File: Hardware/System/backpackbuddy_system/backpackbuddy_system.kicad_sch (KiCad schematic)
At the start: 27 parts, among them J1 PIR, J2 Ultrasonic 2, J3 Ultrasonic 1, J4 Left Vibration 1, J5 Left Vibration 2, J6 Raspberry Pi, J7 ESP8266, J8 Right Vibration 1, J9 Right Vibration 2, Q1 Q_NMOS_GSD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

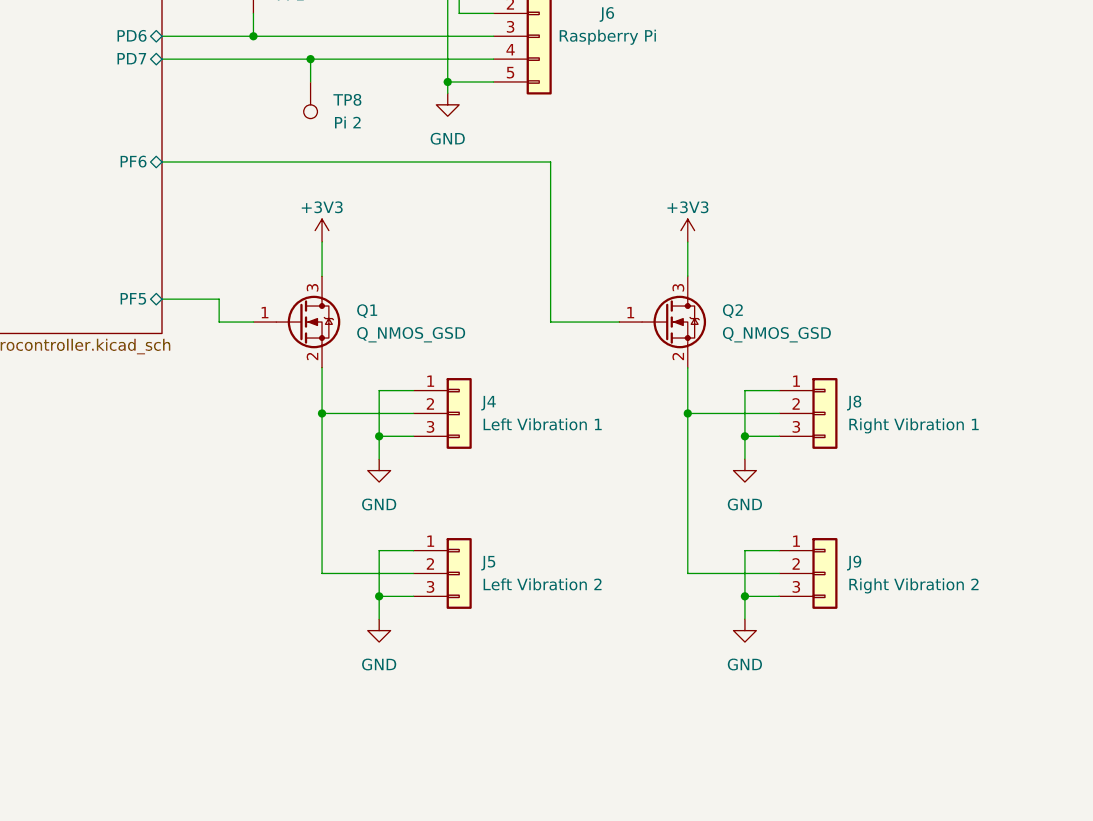
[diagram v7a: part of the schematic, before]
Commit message: changed D1, the MCU reset switch diode from 50V to 1V, changed crystal caps to 22pF
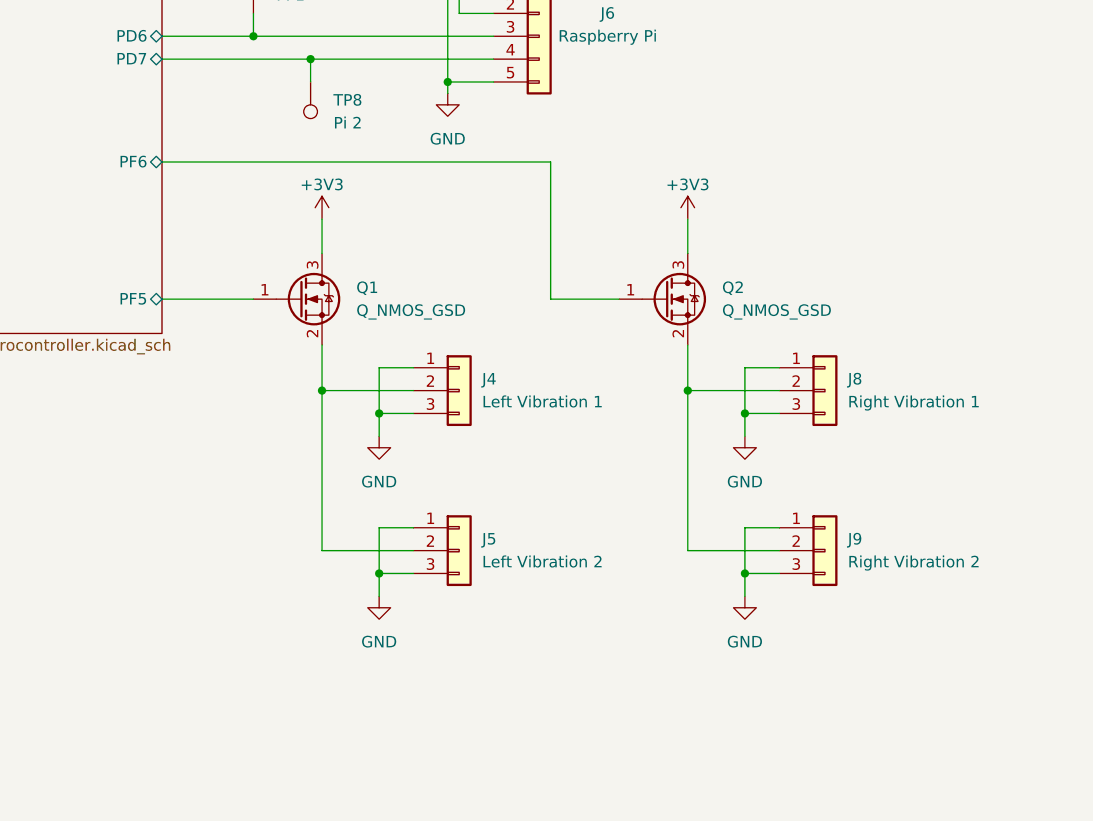
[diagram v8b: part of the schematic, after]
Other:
- moved on the sheet: J4, J5, J8, J9, Q1, Q2
